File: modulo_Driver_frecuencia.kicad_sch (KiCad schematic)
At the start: 24 parts, among them J1 Conn_01x02_Pin, J2 Conn_01x02_Pin, Q1 MJE13009G, Q2 MJE13009G, T1 Transformer_1P_1S

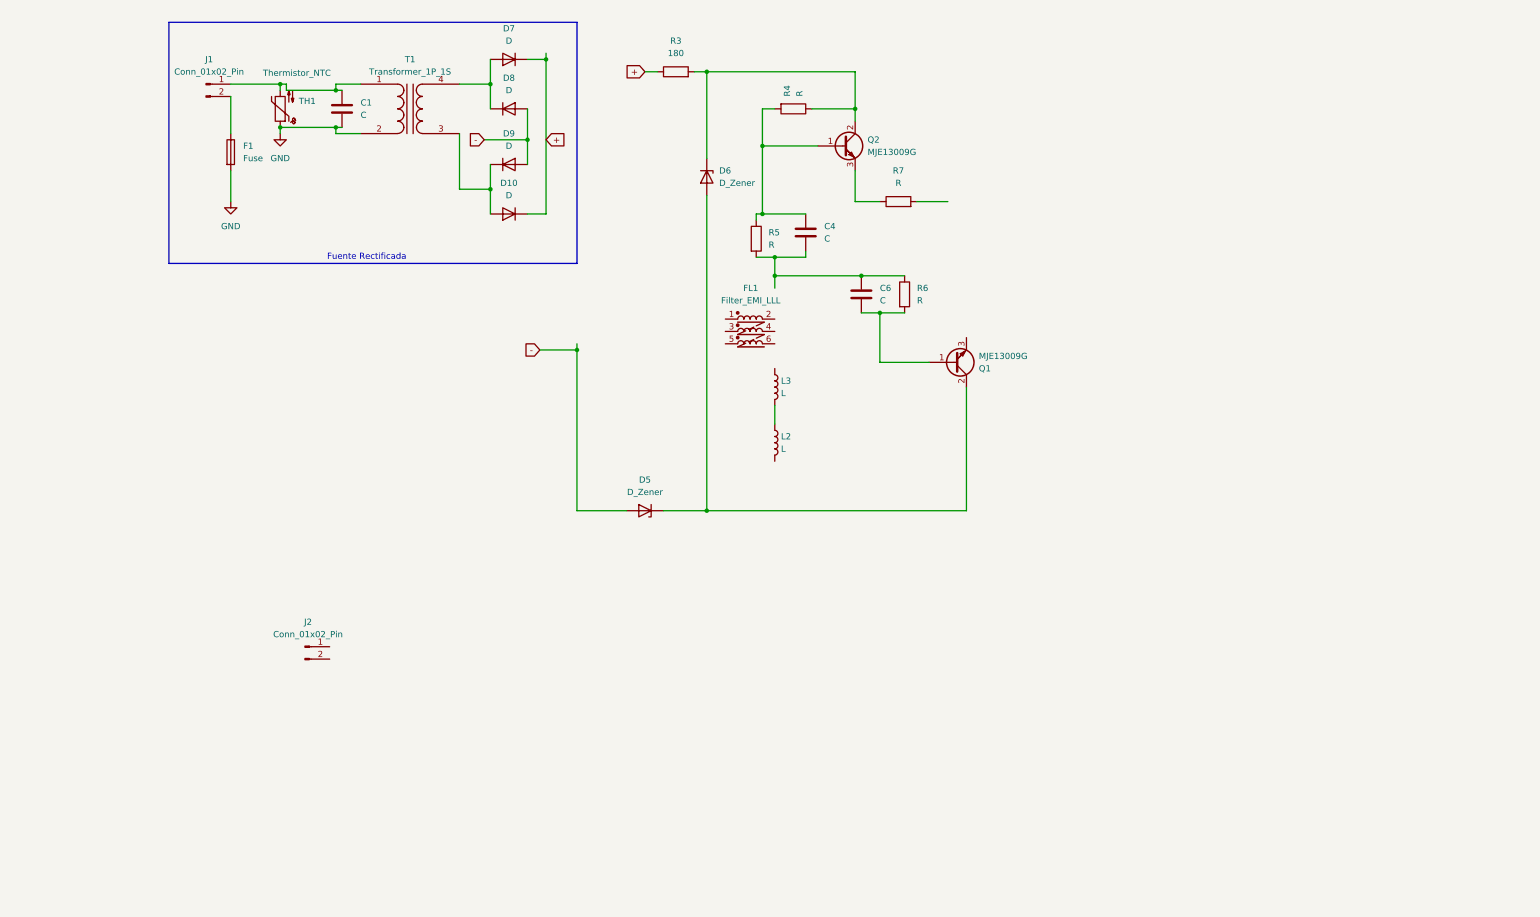
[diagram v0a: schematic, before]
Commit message: modulo de frecuencia agregado, necesita corrección
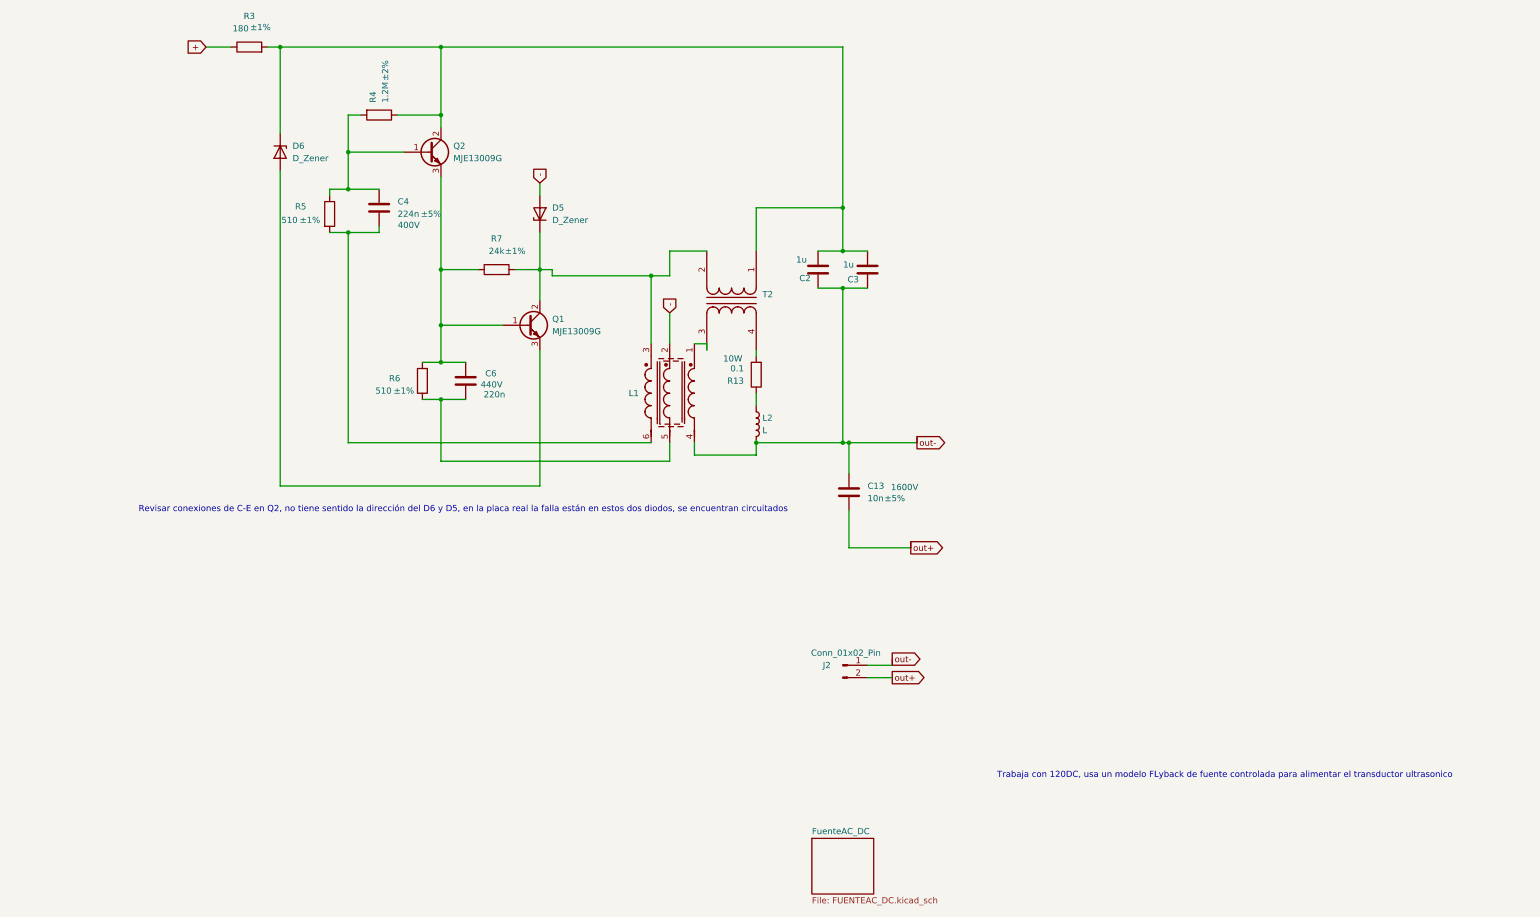
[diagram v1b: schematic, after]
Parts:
- removed C1: C, symbol Device:C
- removed D10, D7, D8, D9: D, symbol Device:D
- removed F1: Fuse, symbol Device:Fuse
- removed FL1: Filter_EMI_LLL, symbol Device:Filter_EMI_LLL
- removed J1: Conn_01x02_Pin, symbol Connector:Conn_01x02_Pin
- removed L3: L, symbol Device:L
- removed T1: Transformer_1P_1S, symbol Device:Transformer_1P_1S
- removed TH1: Thermistor_NTC, symbol Device:Thermistor_NTC
- added C13: 10n, symbol Device:C
- added C2, C3: 1u, symbol Device:C
- added L1: ~, symbol 3Winding-Coupled-Inductor:L
- added R13: 0.1, symbol Device:R
- added T2: Transformer_1P_1S, symbol Device:Transformer_1P_1S
- C4: value C -> 224n; Tol (none) -> ±5%; maxVol (none) -> 400V
- C6: value C -> 220n; maxVol (none) -> 440V
- R3: Tol (none) -> ±1%
- R4: value R -> 1.2M; Tol (none) -> ±2%
- R5, R6: value R -> 510; Tol (none) -> ±1%
- R7: value R -> 24k; Tol (none) -> ±1%
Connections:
- net -: now also L1.2
- net at D6.1 (K), Q2.2 (C), R3.2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: now also C2.2, C3.2, T2.1 (AA)
- net at Q2.3 (E), R7.1: now also C6.2, Q1.1 (B), R6.2
- net at C6.1, R6.1: now also L1.5; no longer C4.1, R5.2
- net at L2.1: now also R13.1
- net at R7.2: now also D5.1 (K), Q1.2 (C), L1.3, T2.2 (AB)
- net out-: now reaches J2.1 (Pin_1)
- net out-: now also L2.2, C13.1, C2.1, C3.1, L1.4
- net out+: now reaches J2.2 (Pin_2)
- net out+: now also C13.2
- net at Q1.3 (E): now also D6.2 (A)
- new net: L1.1, T2.3 (SA)
- new net: R13.2, T2.4 (SB)
- new net: C4.1, L1.6, R5.2
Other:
- added sheet FuenteAC_DC (FUENTEAC_DC.kicad_sch)
- note added: "Revisar conexiones de C-E en Q2, no tiene sentido la dirección del D6 y D5, en la placa real la falla están en estos dos diodos, se encuentran circuitados"
- note added: "Trabaja con 120DC, usa un modelo FLyback de fuente controlada para alimentar el transductor ultrasonico"
- note removed: "Fuente Rectificada"
- moved on the sheet: C4, C6, D6, J2, Q1, Q2, R3, R4, R5, R6, R7

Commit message: 123
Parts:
- removed D5, D6: D_Zener, symbol Device:D_Zener
- added D5: ESH2PB, Diode_SMD:D_SMP_DO-220AA, symbol Diode:ESH2PB
- added D6: RF01VM2S, Diode_SMD:D_SOD-323, symbol Diode:RF01VM2S
- renumbered R13 to R2
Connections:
- net -: now also D5.2 (A)
- net out+: now also L2.2
- net out-: now also R2.1; no longer C2.1, C3.1, L2.2
- net at C2.2, C3.2, Q2.2 (C)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: now also D6.1 (K); no longer T2.1 (AA)
- net at L1.3, Q1.2 (C), R7.2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: now also C2.1, C3.1, D5.1 (K)
- net at L1.1, T2.3 (SA): now also R2.2
- net at T2.4 (SB): now also L2.1; no longer R2.2
- net at Q1.3 (E): now also D6.2 (A)
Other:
- moved on the sheet: C13, C2, C3, L1, Q1, R2, R7
